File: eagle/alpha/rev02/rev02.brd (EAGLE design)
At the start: 100 x 80 mm, 379 parts, among them CN1 HOST, CN2 HOST, IC1 IS45S32160F, IC2 IS45S32160F, IC3 N25Q128A13ES, IC4 N25Q128A13ES, Q1 2N7002, Q3 2N7002, Q5 ASFL1, Q6 2N7002, T1 BC847, T2 BC847, T3 BC818, U1 MC14551BDG, U2 MC74HC1G14DTT1G, U3 ATTINY828R-AU, U4 MC14551BDG, U5 23K640-I/SN, U6 MCP79412-I/SN, U7 XC7A200TFBG484, Y1 12 MHz, Y2 12 MHz

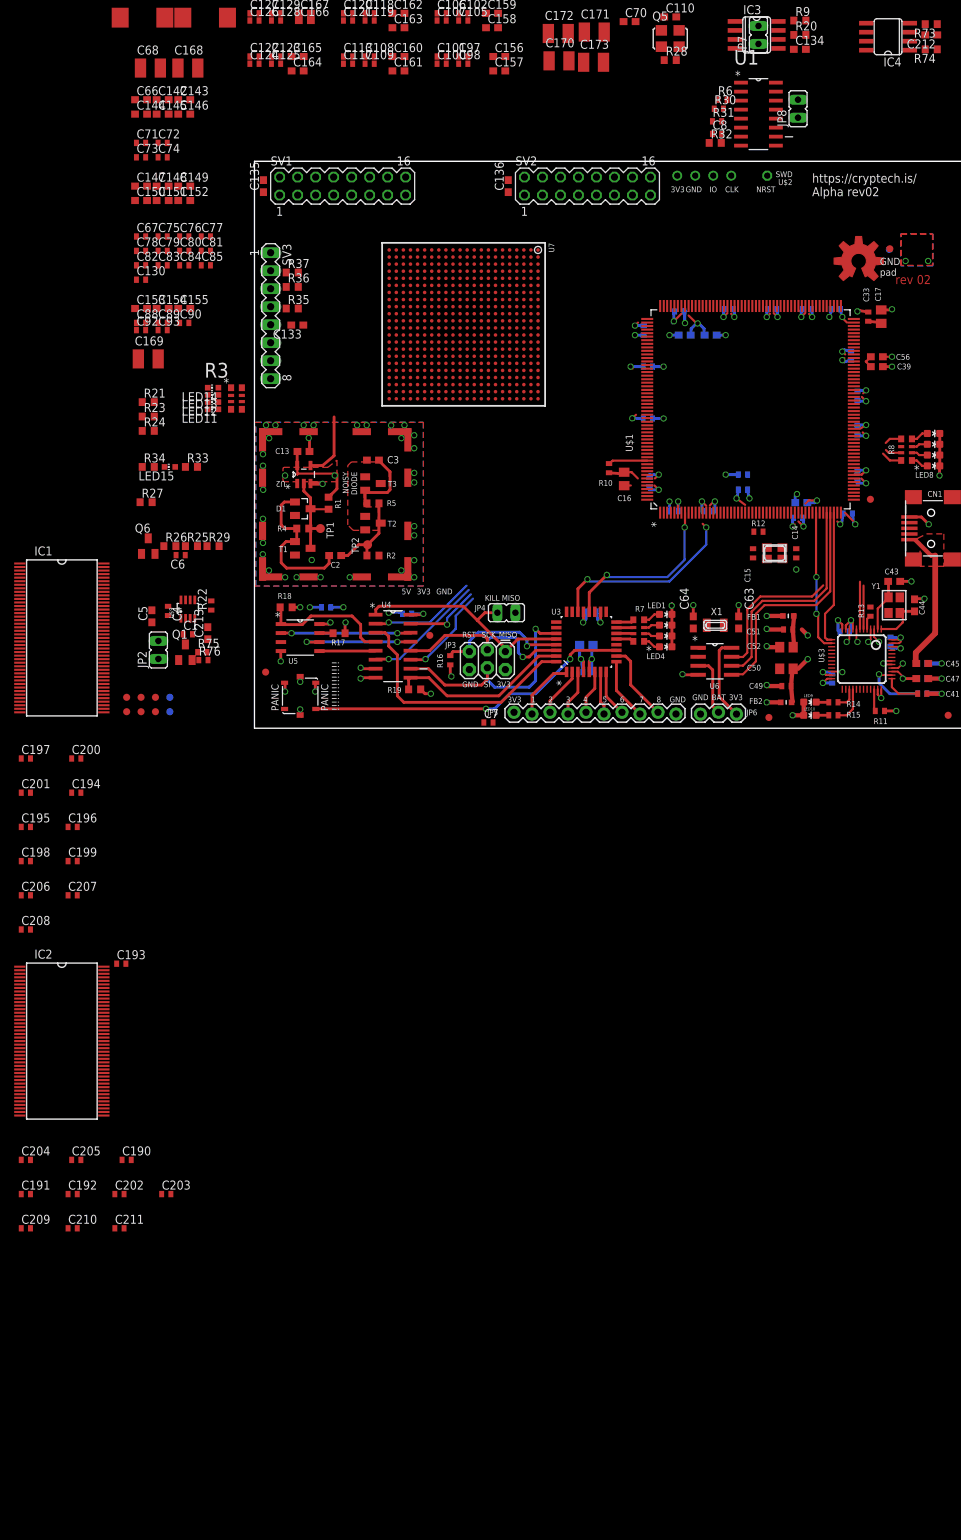
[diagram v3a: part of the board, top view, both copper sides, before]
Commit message: add SPI mux for FPGA cfg memory, and some other minor things.
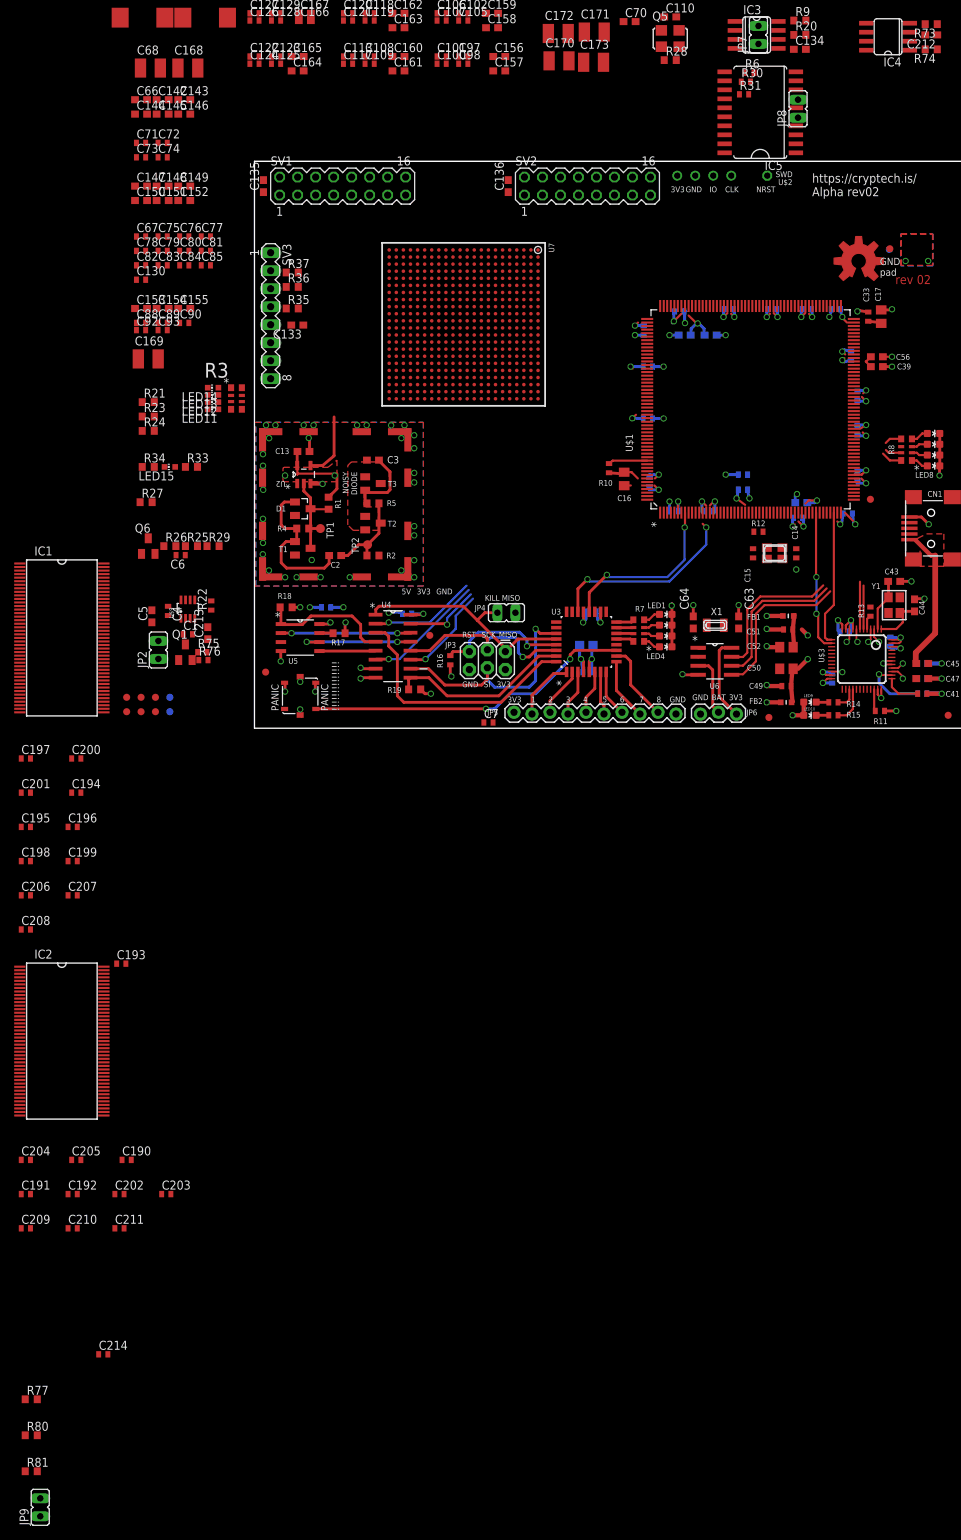
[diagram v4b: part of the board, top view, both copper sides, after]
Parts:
- removed C8: 0.1 uF, resistor:C0402
- removed R32: 15K, resistor:R0603
- removed U1: MC14551BDG, ON_Semiconductor-MC14551BDG:SOIC127P600X175-16N
- added C214: 0.1uF, resistor:C0402
- added IC5: 74AC244DW, 74xx-eu:SO20W
- added JP9: (no value), jumper:JP1
- added R77, R80, R81: 4.7k, resistor:R0603
- moved R31 5.39 mm to (89.2, 90.2)
- moved R6 5.39 mm to (89.9, 93.2)
- moved R30 5.39 mm to (89.4, 91.9)
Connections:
- net ARM_FPGA_CFG_CONTROL renamed FPGA_CFG_CTRL_ARM_ENA
- removed net N$3: JP8.1, R32.2, U1.9
- new net FPGA_CFG_CTRL_FPGA_DIS: JP9.2, U$1.95
- new net FPGA_PROM_CS_N: IC3.1, IC5.18, IC5.9, R77.1, R9.1
- new net SPI_A_TRISTATE: IC5.1, JP8.1, R80.1
- new net SPI_B_TRISTATE: IC5.19, JP9.1, R81.1
- net 3V3_BATT: no longer C8.1, U1.16
- net ARM_FPGA_CFG_CS_N: now also IC5.2, U$1.104; no longer U1.3
- net ARM_FPGA_CFG_MISO: now also IC5.12; no longer U1.1
- net ARM_FPGA_CFG_MOSI: now also IC5.6; no longer U1.10
- net ARM_FPGA_CFG_SCLK: now also IC5.4; no longer U1.12
- net ARM_LED1: now also U$1.65; no longer U$1.69
- net ARM_LED2: now also U$1.66; no longer U$1.68
- net ARM_LED4: now also U$1.68; no longer U$1.66
- net AVR_GPIO_11: now also U$1.9
- net FPGA_CFG_CS_N: now also IC5.11; no longer U1.4
- net FPGA_CFG_MISO: now also IC5.3; no longer U1.14
- net FPGA_CFG_MOSI: now also IC5.15; no longer U1.5
- net FPGA_CFG_SCLK: now also IC5.13; no longer U1.13
- net FPGA_DONE: now also U$1.177; no longer U$1.119
- net FPGA_INIT_B: now also U$1.119; no longer U$1.176
- net FPGA_IRQ_N_0: now also U$1.122; no longer U$1.175
- net FPGA_IRQ_N_1: now also U$1.123; no longer U$1.174
- net FPGA_IRQ_N_2: now also U$1.174; no longer U$1.123
- net FPGA_IRQ_N_3: now also U$1.175; no longer U$1.122
- net FPGA_PROGRAM_B: now also U$1.120; no longer U$1.177
- net FPGA_PROM_MISO: now also IC5.17, IC5.8; no longer U1.15
- net FPGA_PROM_MOSI: now also IC5.14, IC5.5; no longer U1.6
- net FPGA_PROM_SCLK: now also IC5.16, IC5.7; no longer U1.11
- net FT_CTS: now also U$1.44; no longer U$1.43
- net FT_DTR: now also U$1.53
- net FT_MGMT_CTS: now also U$1.146; no longer U$1.145
- net FT_MGMT_DTR: now also U$1.142
- net FT_MGMT_RTS: now also U$1.145; no longer U$1.146
- net FT_MGMT_VPHY: now also C183.1, C184.1, FB4.2
- net FT_RTS: now also U$1.43; no longer U$1.44
- net FT_VPHY: no longer C183.1, C184.1, FB4.2
- net GND: now also C214.2, IC5.10, R81.2; no longer C8.2, R32.1, U1.7, U1.8
- net KSM_PROM_CS_N: no longer IC3.1, R9.1, U1.2
- net VCCO_3V3: now also C214.1, IC5.20, R77.2, R80.2
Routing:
- net RTC_SDA: track 33.8 -> 22.7 mm
- net RTC_SCL: track 32.4 -> 21.7 mm
- net FT_VCC3V3: track 24.6 -> 20.6 mm

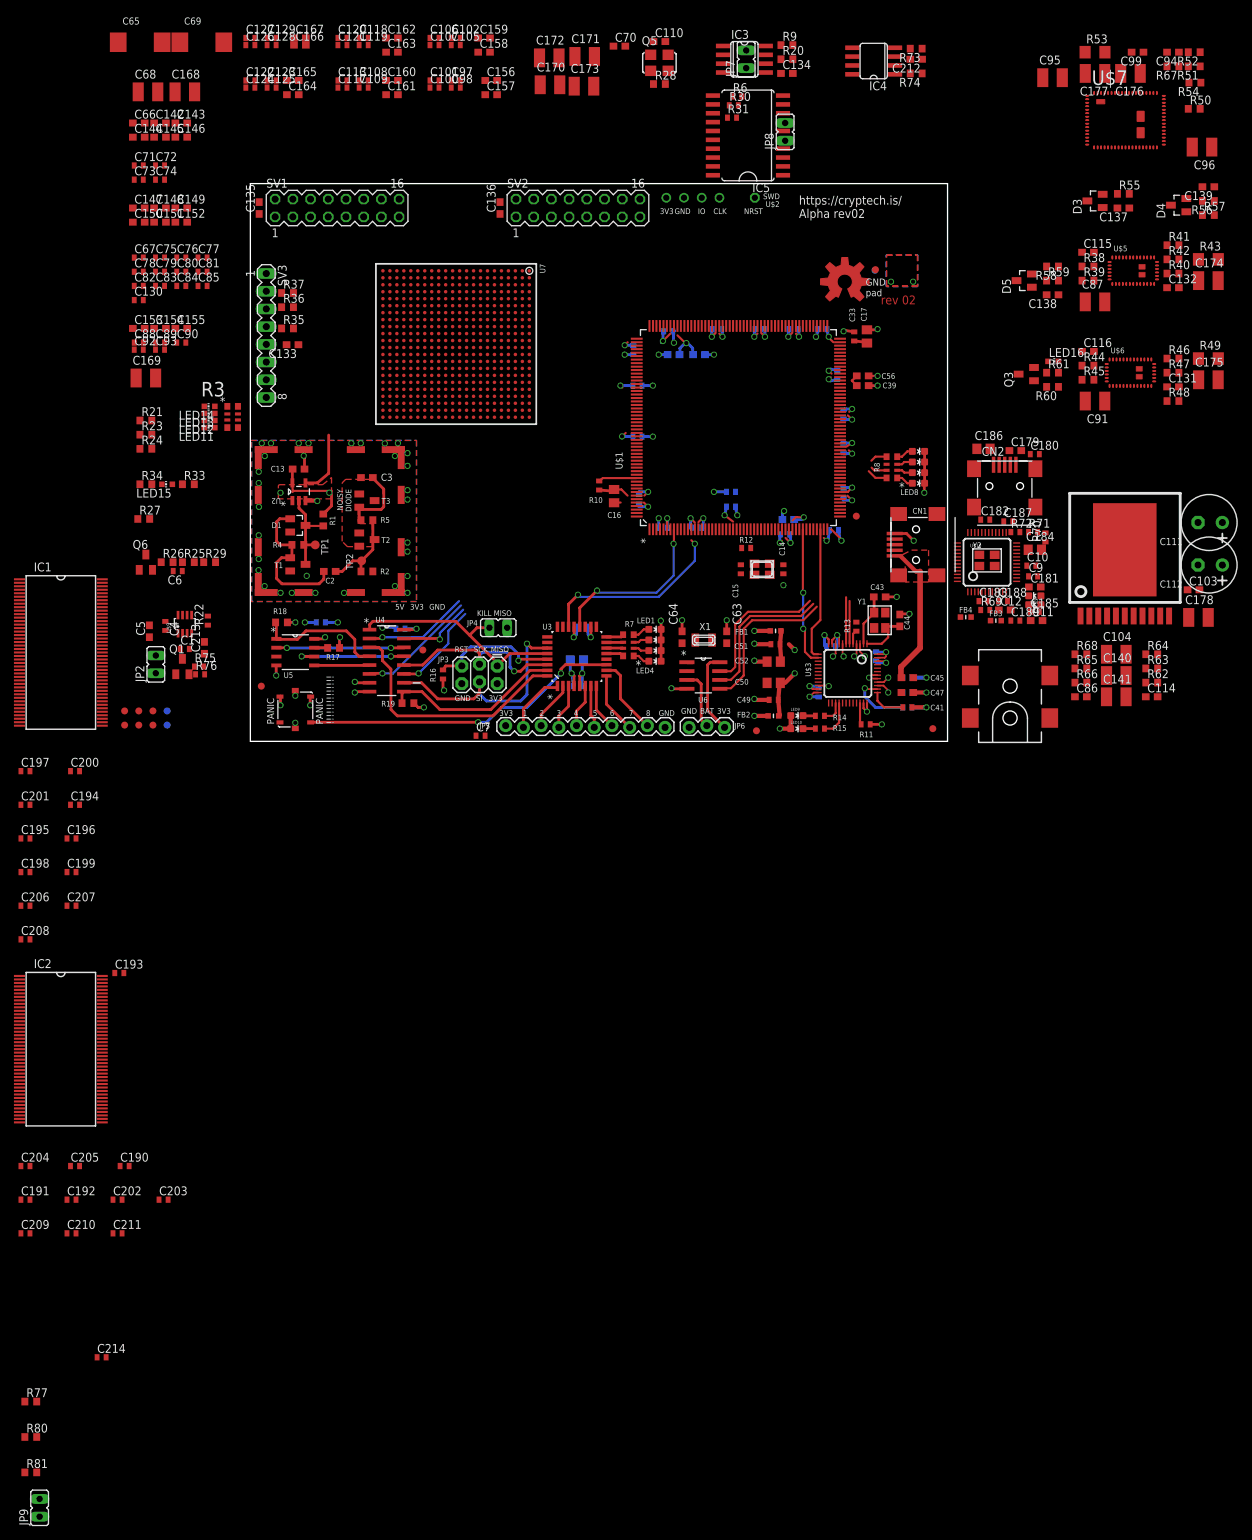
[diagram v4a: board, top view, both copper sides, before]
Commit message: add device prefixes and renumber all components
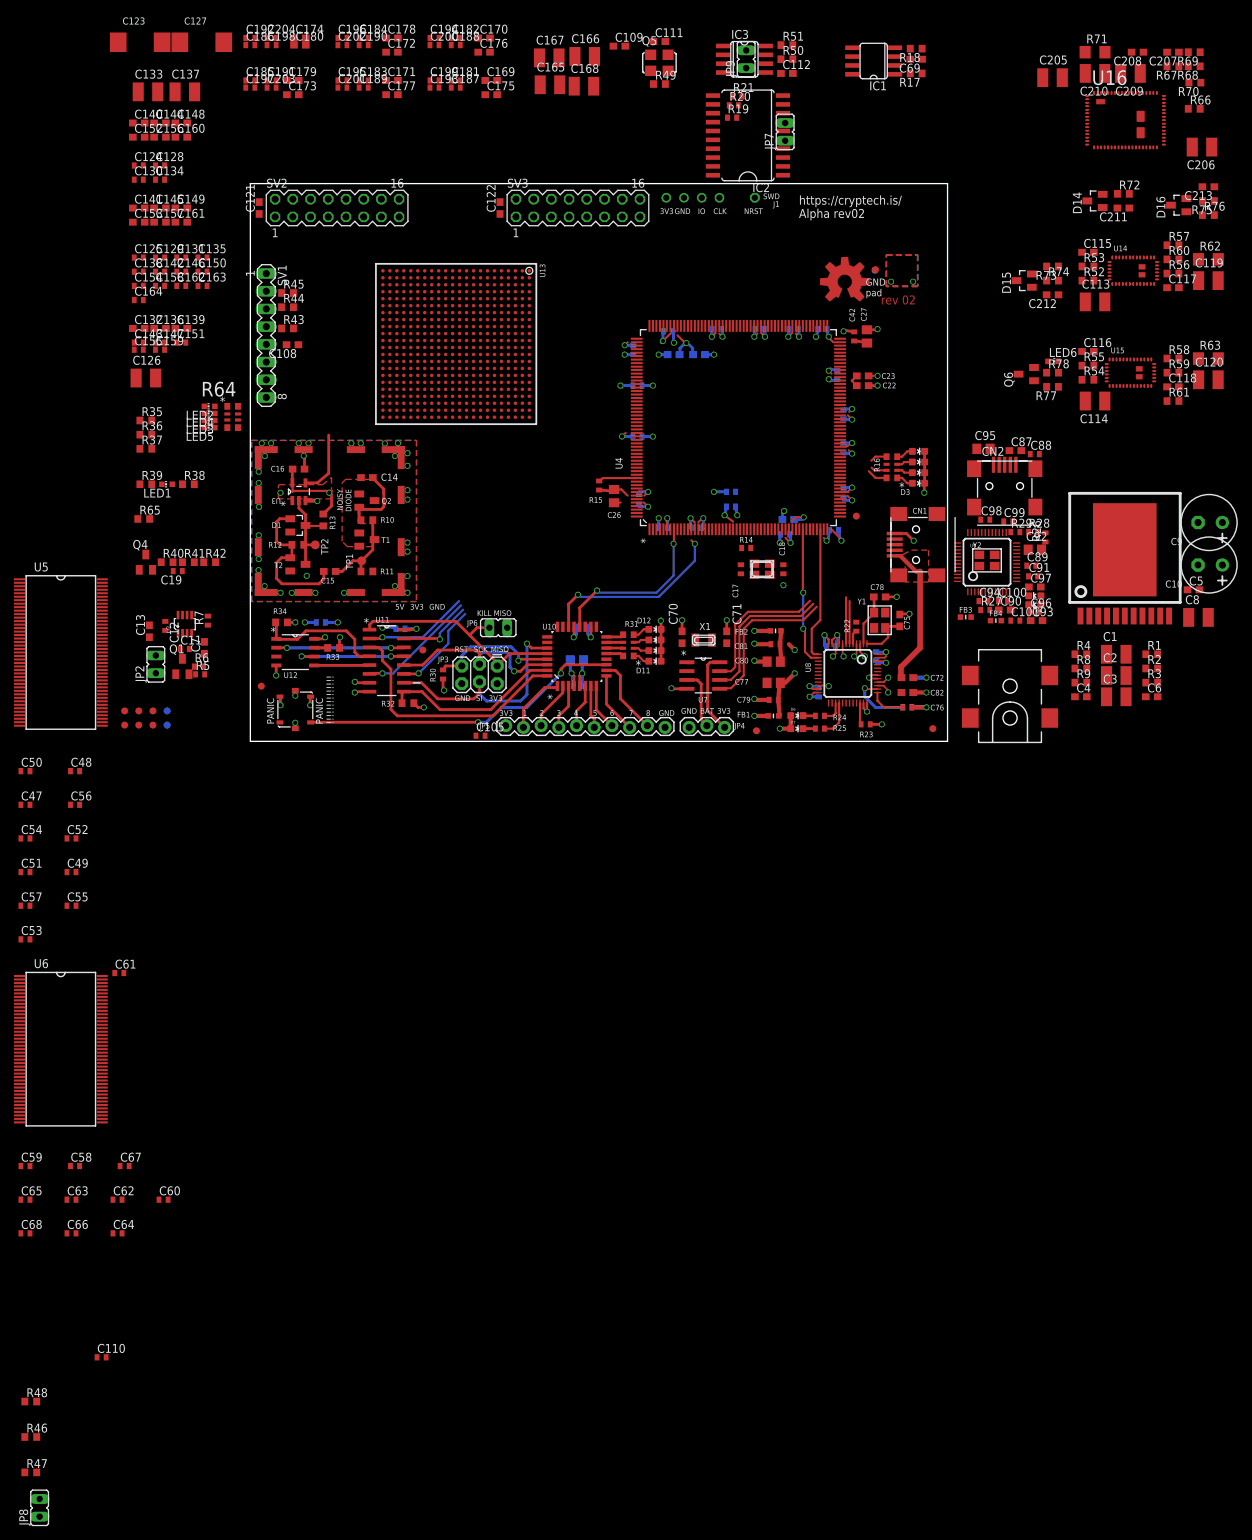
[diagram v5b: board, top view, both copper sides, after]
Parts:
- removed C214: 0.1uF, resistor:C0402
- removed IC4: N25Q128A13ES, altera-configdevices:SO08
- removed IC5: 74AC244DW, 74xx-eu:SO20W
- removed LED11: BLUE, led:CHIP-LED0603
- removed LED12, LED16: GREEN, led:CHIP-LED0603
- removed LED13: YELLOW, led:CHIP-LED0603
- removed LED14, LED15: RED, led:CHIP-LED0603
- removed LED7: YELLOW, SparkFun-LED:LED-0603
- removed LED8: RED, SparkFun-LED:LED-0603
- removed R80, R81: 4.7k, resistor:R0603
- removed U$1: STM32F429BIT6, Alpha-IC:LQFP-208
- removed U$10, U$3: FT232H_SERIAL, FT232H:FT2323HL_LQFP48
- removed U$9: LT3060ITS8-15, Alpha-Power:TSOT-8-23
- added C8: 47 uF, resistor:C1210
- added D10, D2: GREEN, SparkFun-LED:LED-0603
- added D11: RED, SparkFun-LED:LED-0603
- added D12: BLUE, SparkFun-LED:LED-0603
- added D13: YELLOW, SparkFun-LED:LED-0603
- added D14, D15, D16: BAT54, diode:SOT23
- added R32: 15K, resistor:R0603
- added R78: 330, resistor:R0603
- added U10: ATTINY828R-AU, ATMEL-ATTINY828R-AU:QFP80P900X900X120-32N
- added U11: MC14551BDG, ON_Semiconductor-MC14551BDG:SOIC127P600X175-16N
- added U12: 23K640-I/SN, Microchip-23K640-I_SN:SOIC127P600X175-8N
- added U13: XC7A200TFBG484, Xilinx_XC7A200TFBG484:FF484
- added U8, U9: FT232H_SERIAL, Alpha-IC:FT2323HL_LQFP48
- C1: value 10NF -> 10 uF; device rcl:C0402 -> resistor:C1210
- C10, C9: value 0.1 uF -> 330uF; device resistor:C0402 -> rc-master:CE-035X080
- C100, C101, C105, C106, C107, C73, C74, C76, C79, C81, C83, C84, C85, C88, C89, C98: value 0.47 uF -> 0.1 uF
- C102, C77, C80, C92: value 0.47 uF -> 10 uF; device resistor:C0402 -> resistor:C0805
- C103: value 0.47uF -> 0.1 uF; device resistor:C0603 -> resistor:C0402
- C104: value 10 uF -> 0.1 uF; device resistor:C1210 -> resistor:C0402
- C108, C109, C121, C122: value 0.47 uF -> 0.1 uF; device resistor:C0402 -> resistor:C0603
- C11, C12: value 5 pF -> 10NF; device rcl:C0603 -> rcl:C0402
- C110: value 0.01 uF -> 0.1uF; device resistor:C0603 -> resistor:C0402
- C111: value 330uF -> 0.01 uF; device rc-master:CE-035X080 -> resistor:C0603
- C112: value 330uF -> 0.1 uF; device rc-master:CE-035X080 -> resistor:C0603
- C113: value 0.47 uF -> 22 uF; device resistor:C0402 -> resistor:C1210
- C114: value 0.047uF -> 22 uF; device resistor:C0603 -> resistor:C1210
- C117, C118: value 0.47 uF -> 27pF; device resistor:C0402 -> resistor:C0603
- C119, C120, C126: value 0.47 uF -> 47 uF; device resistor:C0402 -> resistor:C1210
- C123, C127: value 0.47 uF -> 330 uF; device resistor:C0402 -> resistor:SMC_D
- C13: value 0.1 uF -> 2.2 uF LowESR; device rcl:C0603 -> resistor:C0603
- C131: value 27pF -> 0.47 uF; device resistor:C0603 -> resistor:C0402
- C132: value 27pF -> 4.7 uF
- C133, C137: value 0.1 uF -> 47 uF; device resistor:C0603 -> resistor:C1210
- C134, C135, C138: value 0.1 uF -> 0.47 uF; device resistor:C0603 -> resistor:C0402
- C136, C139: value 0.1 uF -> 4.7 uF
- C14, C15: value 5 pF -> 0.1 uF; device rcl:C0402 -> rcl:C0603
- C140, C141: value 10 uF -> 4.7 uF; device resistor:C1210 -> resistor:C0603
- C142, C143, C146, C147, C150, C151, C154, C155, C158, C159, C162, C163, C164, C181: value 4.7 uF -> 0.47 uF; device resistor:C0603 -> resistor:C0402
- C16: value 10 uF -> 0.1 uF; device resistor:C0805 -> rcl:C0603
- C165, C166, C167: value 4.7 uF -> 47 uF; device resistor:C0603 -> resistor:C1210
- C169, C170, C171, C172, C173, C174, C175, C176, C177, C178: value 47 uF -> 4.7 uF; device resistor:C1210 -> resistor:C0603
- C17: value 10 uF -> 5 pF; device resistor:C0805 -> rcl:C0402
- C18: value 0.1uF -> 5 pF; device resistor:C0402 -> rcl:C0402
- C180: value 0.1 uF -> 4.7 uF; device resistor:C0402 -> resistor:C0603
- C182, C183, C185, C187, C188, C189, C193, C197, C200, C201, C204: value 0.1 uF -> 0.47 uF
- C184, C186: value 10 uF -> 0.47 uF; device resistor:C0805 -> resistor:C0402
- C190, C191, C192, C194, C195, C196, C198, C199, C202, C203: value 0.1uF -> 0.47 uF
- C2, C3: value 0.1 uF -> 10 uF; device rcl:C0603 -> resistor:C1210
- C205: value 0.1 uF -> 22 uF; device resistor:C0402 -> resistor:C1210
- C206: value 0.1uF -> 22 uF; device resistor:C0402 -> resistor:C1210
- C207, C6: value 0.1uF -> 0.047uF; device resistor:C0402 -> resistor:C0603
- C208: value 0.1uF -> 27pF; device resistor:C0402 -> resistor:C0603
- C209, C210: value 0.1uF -> 47 uF; device resistor:C0402 -> resistor:C1210
- C21: value 0.1uF -> 1 uF; device resistor:C0402 -> resistor:C0603
- C211: value 0.1uF -> 0.1 uF; device resistor:C0402 -> resistor:C0603
- C213: value 2.2 uF LowESR -> 0.1 uF
- C22, C23, C24: value 0.1uF -> 2.2 uF; device resistor:C0402 -> resistor:C0603
- C25: value 0.1 uF -> 2.2 uF; device resistor:C0402 -> resistor:C0603
- C26, C27: value 0.1uF -> 10 uF; device resistor:C0402 -> resistor:C0805
- C30: value 1 uF -> 0.1uF; device resistor:C0603 -> resistor:C0402
- C31: value 0.1uF -> 0.1 uF
- C38, C39, C56, C57: value 2.2 uF -> 0.1uF; device resistor:C0603 -> resistor:C0402
- C4: value 10NF -> 0.047uF; device rcl:C0402 -> resistor:C0603
- C41, C42, C46, C49, C51, C53, C54, C55, C60, C62: value 0.1 uF -> 0.1uF
- C43, C44: value 5 pF -> 0.1uF; device rcl:C0603 -> resistor:C0402
- C45, C66: value 4.7 uF -> 0.1uF; device resistor:C0603 -> resistor:C0402
- C47: value 4.7 uF -> 0.1 uF; device resistor:C0603 -> resistor:C0402
- C5: value 2.2 uF LowESR -> 0.47uF
- C50, C58: value 10 uF -> 0.1 uF; device resistor:C0805 -> resistor:C0402
- C52: value 10 uF -> 0.1uF; device resistor:C0805 -> resistor:C0402
- C63, C64: value 5pF -> 0.1uF; device rcl:C0603 -> resistor:C0402
- C65: value 330 uF -> 0.1uF; device resistor:SMC_D -> resistor:C0402
- C67: value 0.47 uF -> 0.1uF
- C68: value 47 uF -> 0.1uF; device resistor:C1210 -> resistor:C0402
- C69: value 330 uF -> 0.1 uF; device resistor:SMC_D -> resistor:C0603
- C7: value 0.1 uF -> 2.2 uF LowESR; device resistor:C0402 -> resistor:C0603
- C70: value 0.1 uF -> 5pF; device resistor:C0603 -> rcl:C0603
- C71: value 0.47 uF -> 5pF; device resistor:C0402 -> rcl:C0603
- C72, C82, C97: value 0.47 uF -> 4.7 uF; device resistor:C0402 -> resistor:C0603
- C75, C78, C90, C93: value 0.47 uF -> 5 pF; device resistor:C0402 -> rcl:C0603
- C86, C94: value 0.047uF -> 0.1 uF; device resistor:C0603 -> resistor:C0402
- C87: value 22 uF -> 4.7 uF; device resistor:C1210 -> resistor:C0603
- C91, C96: value 22 uF -> 0.1 uF; device resistor:C1210 -> resistor:C0402
- C95: value 22 uF -> 10 uF; device resistor:C1210 -> resistor:C0805
- C99: value 27pF -> 0.1 uF; device resistor:C0603 -> resistor:C0402
- D3: value BAT54 -> RED; device diode:SOT23 -> SparkFun-LED:LED-0603
- D4: value BAT54 -> BLUE; device diode:SOT23 -> SparkFun-LED:LED-0603
- D5: value BAT54 -> YELLOW; device diode:SOT23 -> SparkFun-LED:LED-0603
- IC1: value IS45S32160F -> N25Q128A13ES; device Alpha-IC:TSOP2-86L -> altera-configdevices:SO08
- IC2: value IS45S32160F -> 74AC244DW; device Alpha-IC:TSOP2-86L -> 74xx-eu:SO20W
- JP4: device jumper:JP1 -> SparkFun-Connectors:1X03_LOCK
- JP6: device SparkFun-Connectors:1X03_LOCK -> jumper:JP1
- LED1: value BLUE -> RED; device SparkFun-LED:LED-0603 -> led:CHIP-LED0603
- LED2: value GREEN -> RED; device SparkFun-LED:LED-0603 -> led:CHIP-LED0603
- LED3: value YELLOW -> GREEN; device SparkFun-LED:LED-0603 -> led:CHIP-LED0603
- LED4: value RED -> YELLOW; device SparkFun-LED:LED-0603 -> led:CHIP-LED0603
- LED5, LED6: device SparkFun-LED:LED-0603 -> led:CHIP-LED0603
- Q3: value 2N7002 -> (none); device transistors_gaui:SOT23 -> adafruit:NX3225
- Q4: value (none) -> 2N7002; device adafruit:NX3225 -> transistors_gaui:SOT23
- R1: value 1K -> 56k
- R10: value 10K -> 470; device resistor:R0402 -> resistor:R0603
- R11: value 10K -> 1K; device resistor:R0402 -> resistor:R0603
- R12: value 0 -> 10K; device resistor:R0402 -> resistor:R0603
- R13: value 12K -> 1K; device resistor:R0402 -> resistor:R0603
- R14: value 220 -> 0
- R15: value 220 -> 10K
- R16: value 15K -> 330R; device resistor:R0402 -> Panasonic-EXB-ERJ:RESCAXE80P320X160X60-8N
- R17, R18: value 15K -> 4.7k
- R19: value 15K -> 10K; device resistor:R0603 -> resistor:R0402
- R2: value 1K -> 4.64k
- R20: value 4.7k -> 10K; device resistor:R0603 -> resistor:R0402
- R21, R23, R27: value 1.0k -> 10K; device resistor:R0603 -> resistor:R0402
- R22: value 10K -> 12K
- R24: value 1.0k -> 220; device resistor:R0603 -> resistor:R0402
- R25, R29: value 4.7k -> 220; device resistor:R0603 -> resistor:R0402
- R26: value 4.7k -> 12K; device resistor:R0603 -> resistor:R0402
- R28: value 0 -> 220; device resistor:R0603 -> resistor:R0402
- R3: value 330R -> 100; device Panasonic-EXB-ERJ:RESCAXE80P320X160X60-8N -> resistor:R0603
- R30: value 10K -> 15K
- R31: value 10K -> 330R; device resistor:R0402 -> Panasonic-EXB-ERJ:RESCAXE80P320X160X60-8N
- R33: value 330 -> 15K
- R34: value 100 -> 15K
- R35, R36, R37: value 10k -> 1.0k
- R38: value 62k -> 330
- R39: value 4.7k -> 100
- R4: value 10K -> 0
- R40, R46: value 205k -> 4.7k
- R41: value 147k -> 4.7k
- R42, R48: value 470 -> 4.7k
- R43: value 0 -> 10k; device resistor:R1206 -> resistor:R0603
- R44: value 62k -> 10k
- R45: value 4.7k -> 10k
- R47: value 59k -> 4.7k
- R49: device resistor:R1206 -> resistor:R0603
- R5: value 470 -> 1K; device resistor:R0603 -> resistor:R0402
- R51: value 150k -> 4.7k
- R52: value 226k -> 4.7k
- R53: value 0 -> 62k; device resistor:R1206 -> resistor:R0603
- R54: value 100 -> 4.7k
- R55: value 100k -> 62k
- R56, R58: value 4.7k -> 205k
- R57: value 100k -> 147k
- R59: value 100k -> 59k
- R60: value 4.7k -> 470
- R61: value 330 -> 470
- R62: value 100 -> 0; device resistor:R0603 -> resistor:R1206
- R63: value 4.64k -> 0; device resistor:R0603 -> resistor:R1206
- R64: value 56k -> 330R; device resistor:R0603 -> Panasonic-EXB-ERJ:RESCAXE80P320X160X60-8N
- R65: value 6.3k -> 1.0k
- R66: value 1.21k -> 4.7k
- R68: value 0 -> 150k
- R69: value 10K -> 226k; device resistor:R0402 -> resistor:R0603
- R7: value 330R -> 10K; device Panasonic-EXB-ERJ:RESCAXE80P320X160X60-8N -> resistor:R0402
- R70: value 12K -> 100; device resistor:R0402 -> resistor:R0603
- R71: value 220 -> 0; device resistor:R0402 -> resistor:R1206
- R72: value 220 -> 100k; device resistor:R0402 -> resistor:R0603
- R74: value 4.7k -> 100k
- R75: value 10K -> 4.7k; device resistor:R0402 -> resistor:R0603
- R76: value 1K -> 100k; device resistor:R0402 -> resistor:R0603
- R8: value 330R -> 6.3k; device Panasonic-EXB-ERJ:RESCAXE80P320X160X60-8N -> resistor:R0603
- R9: value 4.7k -> 1.21k
- SV1: device con-lstb:MA08-2 -> con-lstb:MA08-1
- SV3: device con-lstb:MA08-1 -> con-lstb:MA08-2
- U2: value MC74HC1G14DTT1G -> LT3060ITS8-15; device MC74HC1G14DTT1G:SOT95P275X110-5N -> Alpha-Power:TSOT-8-23
- U3: value ATTINY828R-AU -> MC74HC1G14DTT1G; device ATMEL-ATTINY828R-AU:QFP80P900X900X120-32N -> MC74HC1G14DTT1G:SOT95P275X110-5N
- U4: value MC14551BDG -> STM32F429BIT6; device ON_Semiconductor-MC14551BDG:SOIC127P600X175-16N -> Alpha-IC:LQFP-208
- U5: value 23K640-I/SN -> IS45S32160F; device Microchip-23K640-I_SN:SOIC127P600X175-8N -> Alpha-IC:TSOP2-86L
- U6: value MCP79412-I/SN -> IS45S32160F; device MCP79412:SOIC127P600X175-8N -> Alpha-IC:TSOP2-86L
- U7: value XC7A200TFBG484 -> MCP79412-I/SN; device Xilinx_XC7A200TFBG484:FF484 -> MCP79412:SOIC127P600X175-8N
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- renumbered LED10 to D7, LED17 to D8, LED18 to D9, LED9 to D6, T3 to Q2, U$2 to J1, U$4 to S2, U$5 to U14, U$6 to U15, U$7 to U16, U$8 to U1
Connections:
- net 15V_LDO_ENABLE: now also R7.2, U2.7; no longer R22.2, U$9.7
- net 15V_STABLE: now also C11.2, C13.1, R11.1, U2.3, U2.4; no longer C1.2, C5.1, R2.1, U$9.3, U$9.4
- net 3V3_BATT: now also C102.1, C103.1, C104.1, C106.1, C107.1, JP4.2, R30.2, R33.1, R34.2, U10.18, U10.4, U11.16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; no longer C58.1, C59.1, C60.1, C61.1, C62.1, JP6.2, R16.2, R17.1, R18.2, U3.18, U3.4, U4.16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
- net AGND: now also C16.1, T2.2, U3.3; no longer C13.1, T1.2, U2.3
- net AMPLIFIED: now also R12.2, R13.1, T2.3, TP2.TP, U3.2; no longer R1.1, R4.2, T1.3, TP1.TP, U2.2
- net AMP_P1: now also C15.2, R12.1, T2.1; no longer C2.2, R4.1, T1.1
- net ARM_FPGA_CFG_CS_N: now also IC2.2, U4.104; no longer IC5.2, U$1.104
- net ARM_FPGA_CFG_MISO: now also IC2.12, U4.106; no longer IC5.12, U$1.106
- net ARM_FPGA_CFG_MOSI: now also IC2.6, U4.107; no longer IC5.6, U$1.107
- net ARM_FPGA_CFG_SCLK: now also IC2.4, U4.105; no longer IC5.4, U$1.105
- net ARM_LED1: now also R16.5, U4.65; no longer R8.5, U$1.65
- net ARM_LED2: now also R16.6, U4.66; no longer R8.6, U$1.66
- net ARM_LED3: now also R16.7, U4.67; no longer R8.7, U$1.67
- net ARM_LED4: now also R16.8, U4.68; no longer R8.8, U$1.68
- net AVR_GPIO_1: now also U10.1; no longer U3.1
- net AVR_GPIO_10: now also U10.20, U4.8; no longer U$1.8, U3.20
- net AVR_GPIO_11: now also U10.22, U4.9; no longer U$1.9, U3.22
- net AVR_GPIO_2: now also U10.2; no longer U3.2
- net AVR_GPIO_3: now also U10.3; no longer U3.3
- net AVR_GPIO_4: now also U10.6; no longer U3.6
- net AVR_GPIO_5: now also U10.7; no longer U3.7
- net AVR_GPIO_6: now also U10.8; no longer U3.8
- net AVR_GPIO_7: now also U10.9; no longer U3.9
- net AVR_GPIO_8: now also U10.10; no longer U3.10
- net AVR_LED1: now also R31.5, U10.16; no longer R7.5, U3.16
- net AVR_LED2: now also R31.6, U10.15; no longer R7.6, U3.15
- net AVR_LED3: now also R31.7, U10.14; no longer R7.7, U3.14
- net AVR_LED4: now also R31.8, U10.13; no longer R7.8, U3.13
- net AVR_PANIC: now also U10.11; no longer U3.11
- net AVR_RESET: now also R30.1, U10.29; no longer R16.1, U3.29
- net BOOT0: now also R15.2, U4.197; no longer R10.2, U$1.197
- net DIGITIZED_NOISE: now also U13.W19, U3.4; no longer U2.4, U7.W19
- net FMC_A0: now also U13.Y17, U4.16, U5.25, U6.25; no longer IC1.25, IC2.25, U$1.16, U7.Y17
- net FMC_A1: now also U13.Y16, U4.17, U5.26, U6.26; no longer IC1.26, IC2.26, U$1.17, U7.Y16
- net FMC_A10: now also U13.AA14, U4.77, U5.24, U6.24; no longer IC1.24, IC2.24, U$1.77, U7.AA14
- net FMC_A11: now also U13.W14, U4.78, U5.21, U6.21; no longer IC1.21, IC2.21, U$1.78, U7.W14
- net FMC_A12: now also U13.Y14, U4.129, U5.69, U6.69; no longer IC1.69, IC2.69, U$1.129, U7.Y14
- net FMC_A13: now also U13.AB11, U4.130; no longer U$1.130, U7.AB11
- net FMC_A14: now also U13.AB12, U4.131, U5.22, U6.22; no longer IC1.22, IC2.22, U$1.131, U7.AB12
- net FMC_A15: now also U13.AA9, U4.132, U5.23, U6.23; no longer IC1.23, IC2.23, U$1.132, U7.AA9
- net FMC_A16: now also U13.AB10, U4.111; no longer U$1.111, U7.AB10
- net FMC_A17: now also U13.AA10, U4.112; no longer U$1.112, U7.AA10
- net FMC_A18: now also U13.AA11, U4.113; no longer U$1.113, U7.AA11
- net FMC_A19: now also U13.V10, U4.2; no longer U$1.2, U7.V10
- net FMC_A2: now also U13.AA16, U4.18, U5.27, U6.27; no longer IC1.27, IC2.27, U$1.18, U7.AA16
- net FMC_A20: now also U13.W10, U4.3; no longer U$1.3, U7.W10
- net FMC_A21: now also U13.Y11, U4.4; no longer U$1.4, U7.Y11
- net FMC_A22: now also U13.Y12, U4.5; no longer U$1.5, U7.Y12
- net FMC_A23: now also U13.W12, U4.1; no longer U$1.1, U7.W12
- net FMC_A24: now also U13.V13, U4.182; no longer U$1.182, U7.V13
- net FMC_A25: now also U13.V14, U4.183; no longer U$1.183, U7.V14
- net FMC_A3: now also U13.AB16, U4.22, U5.60, U6.60; no longer IC1.60, IC2.60, U$1.22, U7.AB16
- net FMC_A4: now also U13.AB17, U4.23, U5.61, U6.61; no longer IC1.61, IC2.61, U$1.23, U7.AB17
- net FMC_A5: now also U13.AA13, U4.24, U5.62, U6.62; no longer IC1.62, IC2.62, U$1.24, U7.AA13
- net FMC_A6: now also U13.AB13, U4.71, U5.63, U6.63; no longer IC1.63, IC2.63, U$1.71, U7.AB13
- net FMC_A7: now also U13.AA15, U4.74, U5.64, U6.64; no longer IC1.64, IC2.64, U$1.74, U7.AA15
- net FMC_A8: now also U13.AB15, U4.75, U5.65, U6.65; no longer IC1.65, IC2.65, U$1.75, U7.AB15
- net FMC_A9: now also U13.Y13, U4.76, U5.66, U6.66; no longer IC1.66, IC2.66, U$1.76, U7.Y13
- net FMC_CLK: now also U13.W11, U4.167; no longer U$1.167, U7.W11
- net FMC_D0: now also U13.T3, U4.116, U5.2, U6.2; no longer IC1.2, IC2.2, U$1.116, U7.T3
- net FMC_D1: now also U13.T1, U4.117, U5.4, U6.4; no longer IC1.4, IC2.4, U$1.117, U7.T1
- net FMC_D10: now also U13.Y1, U4.87, U5.76, U5.77, U6.76, U6.77; no longer IC1.76, IC1.77, IC2.76, IC2.77, U$1.87, U7.Y1
- net FMC_D11: now also U13.U3, U4.88, U5.79, U6.79; no longer IC1.79, IC2.79, U$1.88, U7.U3
- net FMC_D12: now also U13.V3, U4.89, U5.80, U6.80; no longer IC1.80, IC2.80, U$1.89, U7.V3
- net FMC_D13: now also U13.AA1, U4.108, U5.82, U6.82; no longer IC1.82, IC2.82, U$1.108, U7.AA1
- net FMC_D14: now also U13.AB1, U4.109, U5.83, U6.83; no longer IC1.83, IC2.83, U$1.109, U7.AB1
- net FMC_D15: now also U13.AB3, U4.110, U5.85, U6.85; no longer IC1.85, IC2.85, U$1.110, U7.AB3
- net FMC_D16: now also U13.AB2, U4.98, U5.31, U6.31; no longer IC1.31, IC2.31, U$1.98, U7.AB2
- net FMC_D17: now also U13.Y3, U4.99, U5.33, U6.33; no longer IC1.33, IC2.33, U$1.99, U7.Y3
- net FMC_D18: now also U13.AA3, U4.100, U5.34, U6.34; no longer IC1.34, IC2.34, U$1.100, U7.AA3
- net FMC_D19: now also U13.AA5, U4.101, U5.36, U6.36; no longer IC1.36, IC2.36, U$1.101, U7.AA5
- net FMC_D2: now also U13.U1, U4.164, U5.5, U6.5; no longer IC1.5, IC2.5, U$1.164, U7.U1
- net FMC_D20: now also U13.AB5, U4.102, U5.37, U6.37; no longer IC1.37, IC2.37, U$1.102, U7.AB5
- net FMC_D21: now also U13.Y4, U4.151, U5.39, U6.39; no longer IC1.39, IC2.39, U$1.151, U7.Y4
- net FMC_D22: now also U13.AA4, U4.152, U5.40, U6.40; no longer IC1.40, IC2.40, U$1.152, U7.AA4
- net FMC_D23: now also U13.V4, U4.153, U5.42, U6.42; no longer IC1.42, IC2.42, U$1.153, U7.V4
- net FMC_D24: now also U13.W4, U4.154, U5.45, U6.45; no longer IC1.45, IC2.45, U$1.154, U7.W4
- net FMC_D25: now also U13.R4, U4.155, U5.47, U6.47; no longer IC1.47, IC2.47, U$1.155, U7.R4
- net FMC_D26: now also U13.T4, U4.156, U5.48, U6.48; no longer IC1.48, IC2.48, U$1.156, U7.T4
- net FMC_D27: now also U13.T5, U4.157, U5.50, U6.50; no longer IC1.50, IC2.50, U$1.157, U7.T5
- net FMC_D28: now also U13.U5, U4.207, U5.51, U6.51; no longer IC1.51, IC2.51, U$1.207, U7.U5
- net FMC_D29: now also U13.W6, U4.208, U5.53, U6.53; no longer IC1.53, IC2.53, U$1.208, U7.W6
- net FMC_D3: now also U13.U2, U4.165, U5.7, U6.7; no longer IC1.7, IC2.7, U$1.165, U7.U2
- net FMC_D30: now also U13.W5, U4.11, U5.54, U6.54; no longer IC1.54, IC2.54, U$1.11, U7.W5
- net FMC_D31: now also U13.U6, U4.12, U5.56, U6.56; no longer IC1.56, IC2.56, U$1.12, U7.U6
- net FMC_D4: now also U13.V2, U4.79, U5.8, U6.8; no longer IC1.8, IC2.8, U$1.79, U7.V2
- net FMC_D5: now also U13.R3, U4.80, U5.10, U6.10; no longer IC1.10, IC2.10, U$1.80, U7.R3
- net FMC_D6: now also U13.R2, U4.81, U5.11, U6.11; no longer IC1.11, IC2.11, U$1.81, U7.R2
- net FMC_D7: now also U13.W2, U4.84, U5.13, U6.13; no longer IC1.13, IC2.13, U$1.84, U7.W2
- net FMC_D8: now also U13.Y2, U4.85, U5.74, U6.74; no longer IC1.74, IC2.74, U$1.85, U7.Y2
- net FMC_D9: now also U13.W1, U4.86; no longer U$1.86, U7.W1
- net FMC_NBL0: now also U4.200, U5.16, U6.16; no longer IC1.16, IC2.16, U$1.200
- net FMC_NBL1: now also U4.201, U5.71, U6.71; no longer IC1.71, IC2.71, U$1.201
- net FMC_NBL2: now also U4.205, U5.28, U6.28; no longer IC1.28, IC2.28, U$1.205
- net FMC_NBL3: now also U4.206, U5.59, U6.59; no longer IC1.59, IC2.59, U$1.206
- net FMC_NE1: now also U13.V5, U4.173; no longer U$1.173, U7.V5
- net FMC_NL: now also U13.R6, U4.196; no longer U$1.196, U7.R6
- net FMC_NOE: now also U13.T6, U4.168; no longer U$1.168, U7.T6
- net FMC_NWAIT: now also U13.Y6, U4.172; no longer U$1.172, U7.Y6
- net FMC_NWE: now also U13.AA6, U4.169; no longer U$1.169, U7.AA6
- net FMC_SDCKE0: now also U4.38, U5.67; no longer IC1.67, U$1.38
- net FMC_SDCKE1: now also U4.194, U6.67; no longer IC2.67, U$1.194
- net FMC_SDCLK: now also U4.135, U5.68, U6.68; no longer IC1.68, IC2.68, U$1.135
- net FMC_SDNCAS: now also U4.191, U5.18, U6.18; no longer IC1.18, IC2.18, U$1.191
- net FMC_SDNE0: now also U4.37, U5.20; no longer IC1.20, U$1.37
- net FMC_SDNE1: now also U4.195, U6.20; no longer IC2.20, U$1.195
- net FMC_SDNRAS: now also U4.70, U5.19, U6.19; no longer IC1.19, IC2.19, U$1.70
- net FMC_SDNWE: now also U4.35, U5.17, U6.17; no longer IC1.17, IC2.17, U$1.35
- net FPGA_CFG_CS_N: now also IC2.11, U13.T19; no longer IC5.11, U7.T19
- net FPGA_CFG_CTRL_ARM_ENA: now also JP7.2, U4.118; no longer JP8.2, U$1.118
- net FPGA_CFG_CTRL_FPGA_DIS: now also JP8.2, U4.95; no longer JP9.2, U$1.95
- net FPGA_CFG_MISO: now also IC2.3, U13.R22; no longer IC5.3, U7.R22
- net FPGA_CFG_MOSI: now also IC2.15, U13.P22; no longer IC5.15, U7.P22
- net FPGA_CFG_SCLK: now also IC2.13, U13.L12; no longer IC5.13, U7.L12
- net FPGA_DONE: now also R39.1, U4.177; no longer R34.1, U$1.177
- net FPGA_DONE_INT: now also LED1.C, R39.2, U13.G11; no longer LED15.C, R34.2, U7.G11
- net FPGA_ENTROPY_DISABLE: now also R5.1, U13.B18; no longer R76.1, U7.B18
- net FPGA_GCLK: now also U13.D17; no longer U7.D17
- net FPGA_GPIO_A_0: now also SV2.7, U13.C15; no longer SV1.7, U7.C15
- net FPGA_GPIO_A_1: now also SV2.8, U13.E13; no longer SV1.8, U7.E13
- net FPGA_GPIO_A_2: now also SV2.9, U13.E14; no longer SV1.9, U7.E14
- net FPGA_GPIO_A_3: now also SV2.10, U13.E16; no longer SV1.10, U7.E16
- net FPGA_GPIO_A_4: now also SV2.13, U13.D16; no longer SV1.13, U7.D16
- net FPGA_GPIO_A_5: now also SV2.14, U13.D14; no longer SV1.14, U7.D14
- net FPGA_GPIO_A_6: now also SV2.15, U13.D15; no longer SV1.15, U7.D15
- net FPGA_GPIO_A_7: now also SV2.16, U13.B15; no longer SV1.16, U7.B15
- net FPGA_GPIO_B_0: now also SV3.7, U13.B16; no longer SV2.7, U7.B16
- net FPGA_GPIO_B_1: now also SV3.8, U13.C13; no longer SV2.8, U7.C13
- net FPGA_GPIO_B_2: now also SV3.9, U13.B13; no longer SV2.9, U7.B13
- net FPGA_GPIO_B_3: now also SV3.10, U13.A15; no longer SV2.10, U7.A15
- net FPGA_GPIO_B_4: now also SV3.13, U13.A16; no longer SV2.13, U7.A16
- net FPGA_GPIO_B_5: now also SV3.14, U13.A13; no longer SV2.14, U7.A13
- net FPGA_GPIO_B_6: now also SV3.15, U13.A14; no longer SV2.15, U7.A14
- net FPGA_GPIO_B_7: now also SV3.16, U13.B17; no longer SV2.16, U7.B17
- net FPGA_GPIO_LED_0: now also R64.4, U13.T20; no longer R3.4, U7.T20
- net FPGA_GPIO_LED_1: now also R64.3, U13.W21; no longer R3.3, U7.W21
- net FPGA_GPIO_LED_2: now also R64.2, U13.W22; no longer R3.2, U7.W22
- net FPGA_GPIO_LED_3: now also R64.1, U13.AA20; no longer R3.1, U7.AA20
- net FPGA_GPIO_TAMPER_0: now also U10.25, U13.F15; no longer U3.25, U7.F15
- net FPGA_GPIO_TAMPER_1: now also U10.26, U13.F13; no longer U3.26, U7.F13
- net FPGA_INIT_B: now also Q4.1, R42.2, U4.119; no longer Q6.1, R29.2, U$1.119
- net FPGA_INIT_B_INT: now also Q4.3, R40.1, U13.U12; no longer Q6.3, R26.1, U7.U12
- net FPGA_IRQ_N_0: now also U13.F14, U4.122; no longer U$1.122, U7.F14
- net FPGA_IRQ_N_1: now also U13.F16, U4.123; no longer U$1.123, U7.F16
- net FPGA_IRQ_N_2: now also U13.E17, U4.174; no longer U$1.174, U7.E17
- net FPGA_IRQ_N_3: now also U13.C14, U4.175; no longer U$1.175, U7.C14
- net FPGA_JTAG_TCK: now also R45.1, SV1.2, U13.V12; no longer R37.1, SV3.2, U7.V12
- net FPGA_JTAG_TDI: now also R43.1, SV1.4, U13.R13; no longer R35.1, SV3.4, U7.R13
- net FPGA_JTAG_TDO: now also SV1.5, U13.U13; no longer SV3.5, U7.U13
- net FPGA_JTAG_TMS: now also R44.1, SV1.3, U13.T13; no longer R36.1, SV3.3, U7.T13
- net FPGA_M0: now also R37.1, U13.U11; no longer R24.1, U7.U11
- net FPGA_M1: now also R36.2, U13.U10; no longer R23.2, U7.U10
- net FPGA_M2: now also R35.2, U13.U9; no longer R21.2, U7.U9
- net FPGA_PROGRAM_B: now also R41.1, U13.N12, U4.120; no longer R25.1, U$1.120, U7.N12
- net FPGA_PROM_CS_N: now also IC2.18, IC2.9, R48.1, R51.1; no longer IC5.18, IC5.9, R77.1, R9.1
- net FPGA_PROM_MISO: now also IC2.17, IC2.8; no longer IC5.17, IC5.8
- net FPGA_PROM_MOSI: now also IC2.14, IC2.5; no longer IC5.14, IC5.5
- net FPGA_PROM_SCLK: now also IC2.16, IC2.7; no longer IC5.16, IC5.7
- net FPGA_PROM_W_N: now also JP9.1, R50.2; no longer JP7.1, R20.2
- net FPGA_VCCAUX_1V8: now also C109.1, C126.1, C132.1, C136.1, C139.1, C143.1, C147.1, C151.1, C159.1, R62.2, U13.H12, U13.K10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; no longer C153.1, C154.1, C169.1, C70.1, C88.1, C89.1, C90.1, C92.1, C93.1, R43.2, U7.H12, U7.K10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
- net FPGA_VCCINT_1V0: now also C123.+, C124.1, C125.1, C127.+, C128.1, C129.1, C131.1, C133.1, C134.1, C135.1, C137.1, C138.1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; no longer C143.1, C147.1, C151.1, C168.1, C65.+, C66.1, C67.1, C68.1, C69.+, C71.1, C72.1, C73.1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
- net FT_CTS: now also U4.44, U8.16; no longer U$1.44, U$3.16
- net FT_DTR: now also U4.53, U8.17; no longer U$1.53, U$3.17
- net FT_MGMT_CTS: now also U4.146, U9.16; no longer U$1.146, U$10.16
- net FT_MGMT_DTR: now also U4.142, U9.17; no longer U$1.142, U$10.17
- net FT_MGMT_RTS: now also U4.145, U9.15; no longer U$1.145, U$10.15
- net FT_MGMT_RXD: now also U4.143, U9.14; no longer U$1.143, U$10.14
- net FT_MGMT_TXD: now also U4.144, U9.13; no longer U$1.144, U$10.13
- net FT_MGMT_VCC3V3: now also C100.1, C101.1, C97.1, C98.1, C99.1, R27.2, U9.12, U9.24, U9.39, U9.46; no longer C181.1, C182.1, C187.1, C188.1, C189.1, R69.2, U$10.12, U$10.24, U$10.39, U$10.46
- net FT_MGMT_VPHY: now also C92.1, C94.1, FB3.2, U9.3; no longer C183.1, C184.1, FB4.2, U$10.3
- net FT_MGMT_VPLL: now also C95.1, C96.1, FB4.2, U9.8; no longer C185.1, C186.1, FB3.2, U$10.8
- net FT_MGMT_VREGIN: now also C87.1, C88.1, U9.40; no longer C179.1, C180.1, U$10.40
- net FT_REF: now also R22.1, U8.5; no longer R13.1, U$3.5
- net FT_REF1: now also R26.1, U9.5; no longer R70.1, U$10.5
- net FT_RESET: now also R23.1, U8.34; no longer R11.1, U$3.34
- net FT_RESET1: now also R27.1, U9.34; no longer R69.1, U$10.34
- net FT_RTS: now also U4.43, U8.15; no longer U$1.43, U$3.15
- net FT_RXD: now also U4.45, U8.14; no longer U$1.45, U$3.14
- net FT_RXLED: now also R24.2, U8.27; no longer R14.2, U$3.27
- net FT_RXLED1: now also R28.2, U9.27; no longer R71.2, U$10.27
- net FT_TXD: now also U4.50, U8.13; no longer U$1.50, U$3.13
- net FT_TXLED: now also R25.2, U8.28; no longer R15.2, U$3.28
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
